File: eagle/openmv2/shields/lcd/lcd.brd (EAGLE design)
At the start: 37.8 x 47.5 mm, 12 parts, among them J1 1X8, J2 1X8, Q1 MOSFET

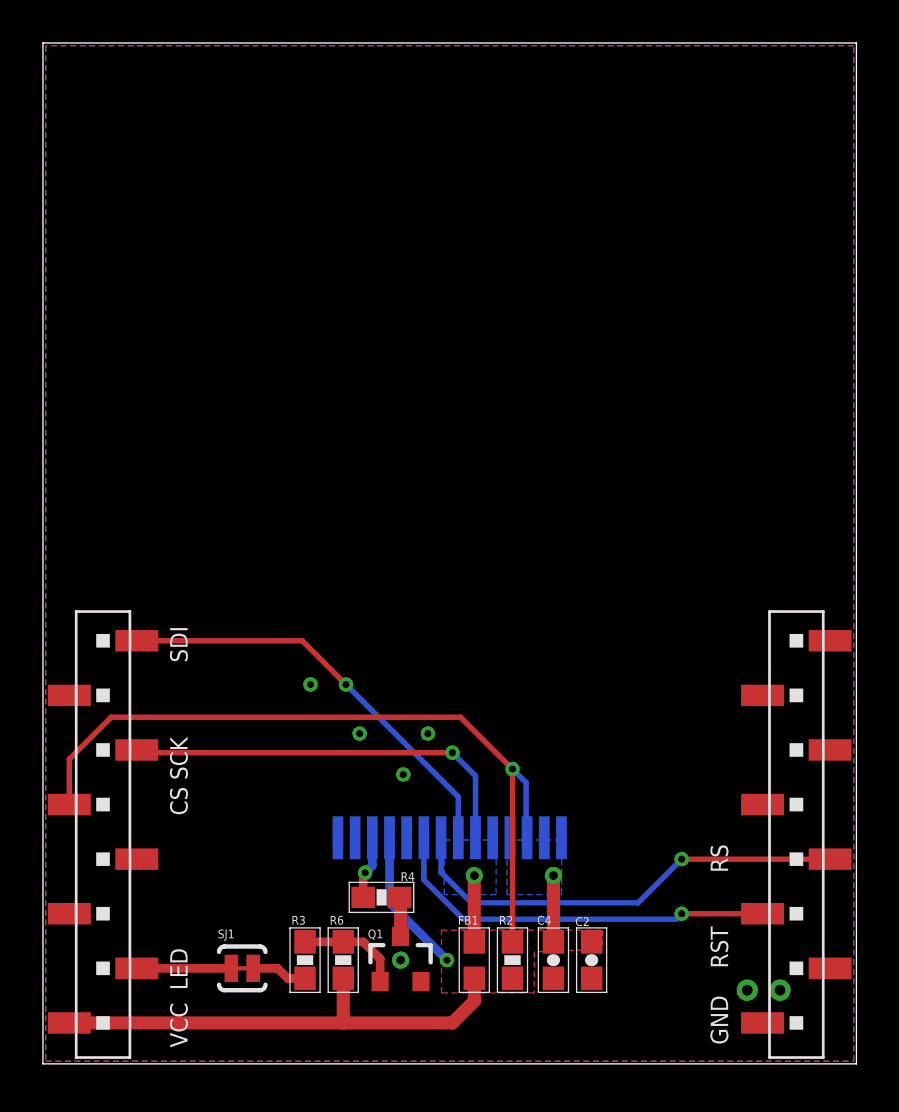
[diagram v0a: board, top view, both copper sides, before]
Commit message: Update shields silk-screen.
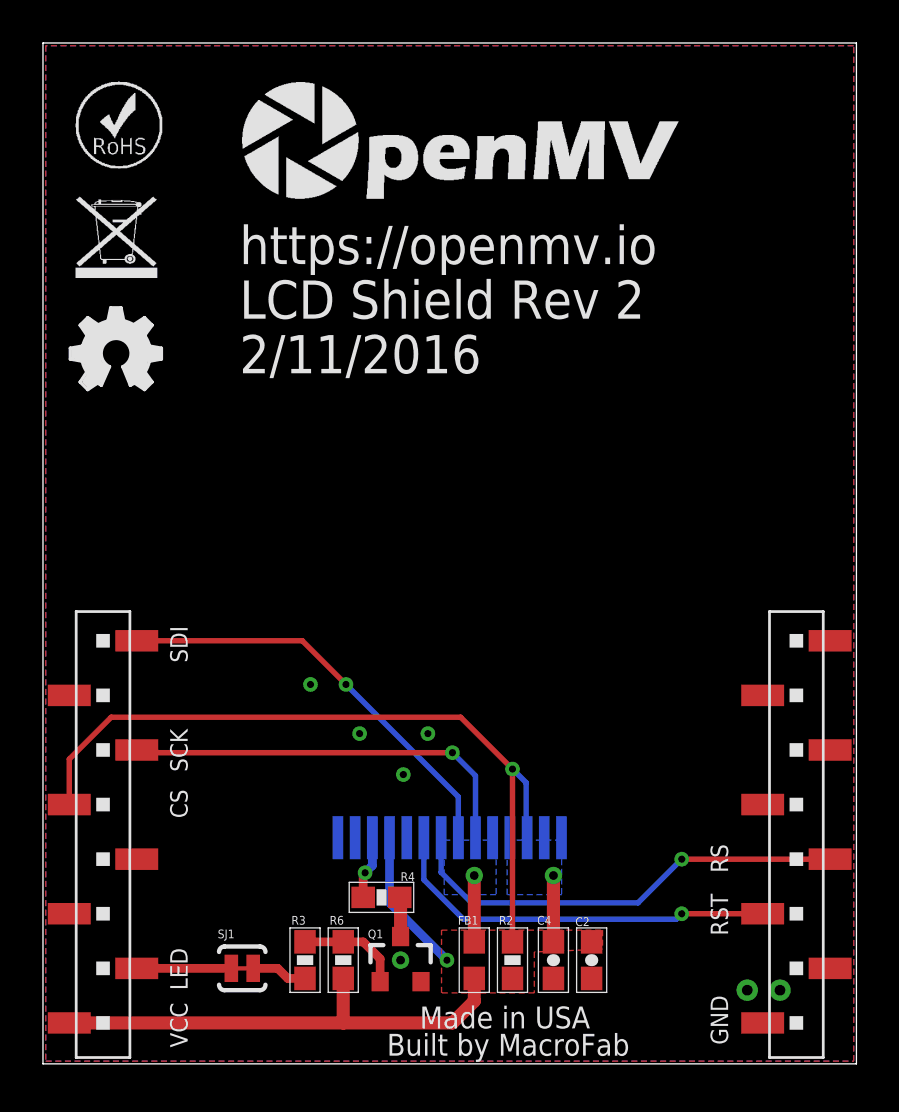
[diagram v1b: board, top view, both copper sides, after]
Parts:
- added U$2: (no value), openmv:ROHS
- added U$3: (no value), openmv:WEEE
- added U$4: (no value), openmv:OMV-LOGO-BIG
- added U$5: (no value), iofault:OSHW_FILLX150_NOTEXT
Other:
- board text added: "2/11/2016"
- board text added: "Built by MacroFab"
- board text added: "LCD Shield Rev 2"
- board text added: "Made in USA"
- board text added: "https://openmv.io"
- board text removed: "0.5 oz copper"
- board text removed: "1 oz copper"
- board text removed: "47 mil core"
- board text removed: "6.7 mil prepreg"
- board text removed: "Antenna trace 12mils (50Ohms impedance)"
- board text removed: "Stackup:"
- board text removed: "er is 3.66"
